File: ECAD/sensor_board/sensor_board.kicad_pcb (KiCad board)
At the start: 2 copper layers, 33 parts, among them J2 Conn_01x04, J4 S4B-XH-SM4-TB, Q2 Q_PMOS_GSD, Q3 Q_PMOS_GSD, Q4 2N7002, U1 TPL5111, U2 TPS22917DBV, U3 TC2030, U4 BC805M, Y1 32.768kHz

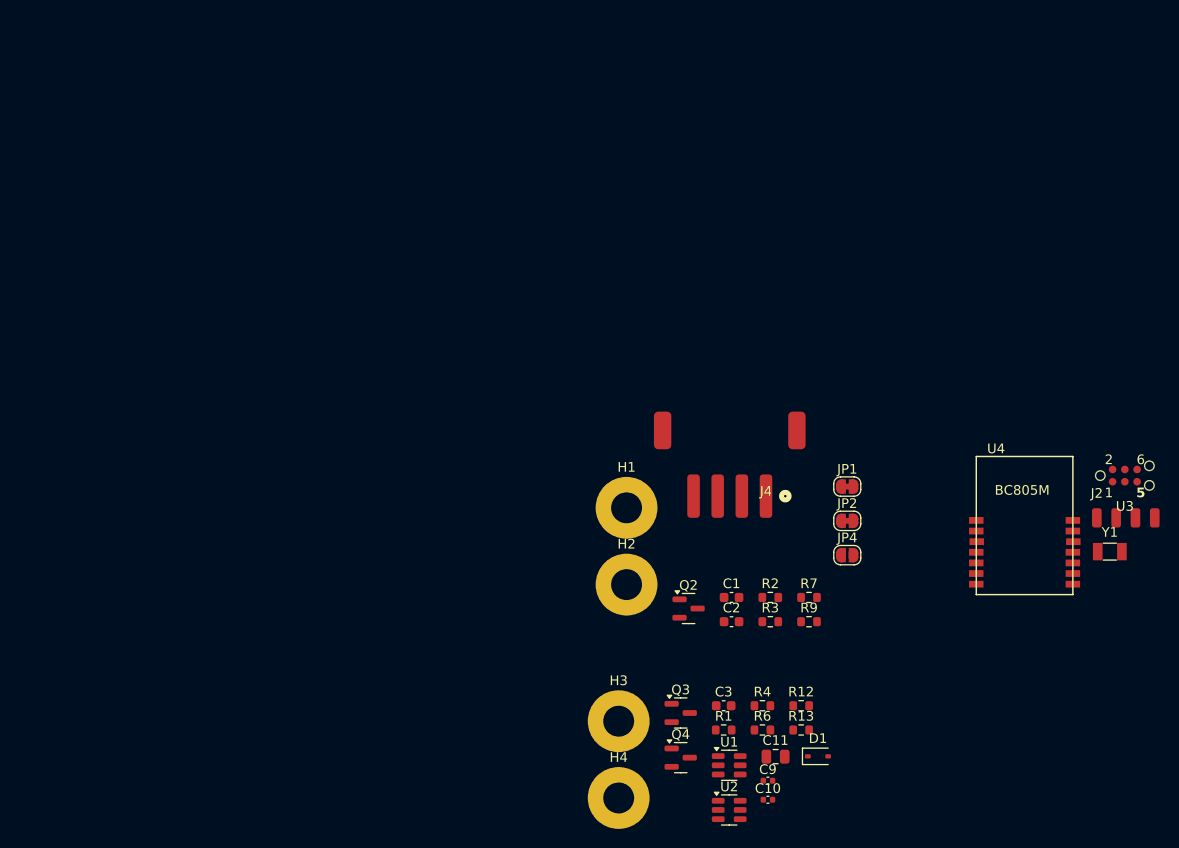
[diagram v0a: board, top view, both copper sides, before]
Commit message: Initial version of routed board
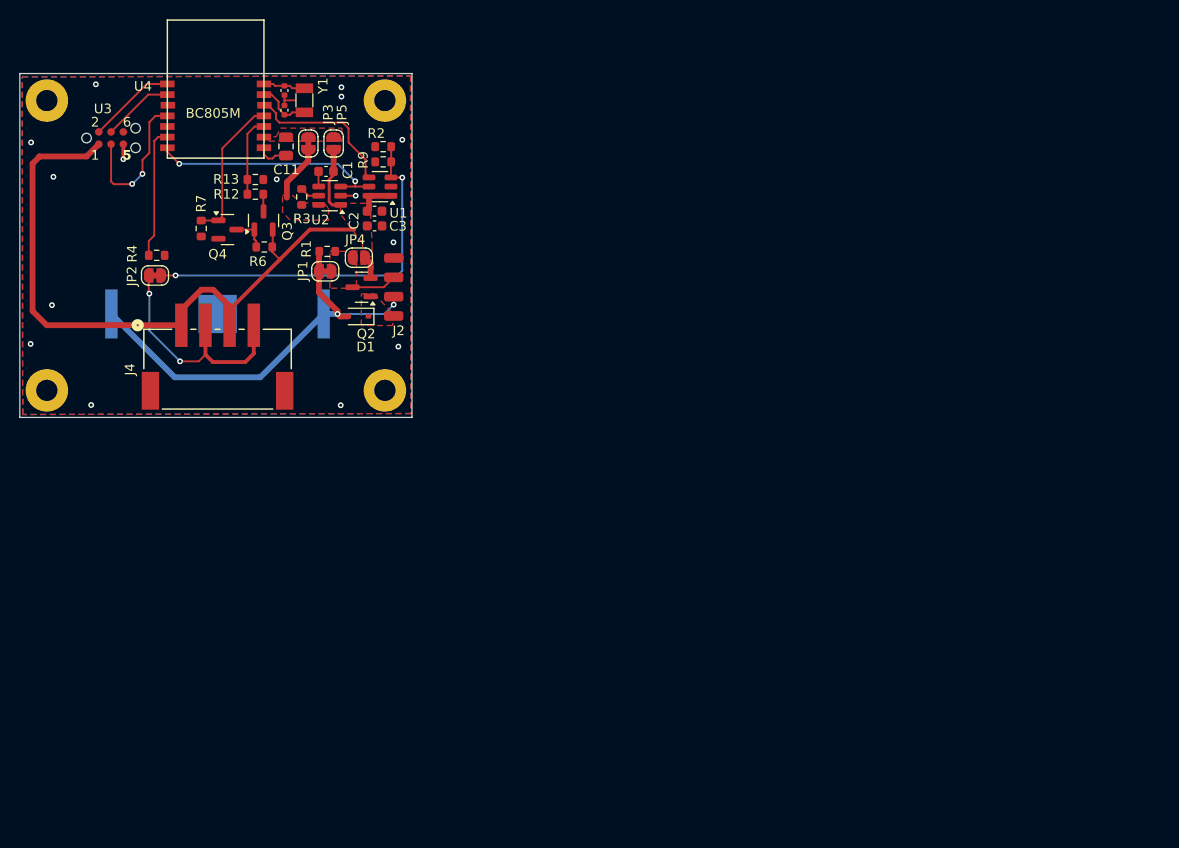
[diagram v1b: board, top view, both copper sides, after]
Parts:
- added BT2: 3034TR, 3034TR:BAT_3034TR, B.Cu at (20.5, 24.9)
- added JP3: ~, Jumper:SolderJumper-2_P1.3mm_Bridged_RoundedPad1.0x1.5mm, F.Cu at (29.9, 7.24)
- added JP5: ~, Jumper:SolderJumper-2_P1.3mm_Open_RoundedPad1.0x1.5mm, F.Cu at (32.5, 7.24)
- H1, H2, H3, H4: footprint MountingHole:MountingHole_3.2mm_M3_Pad -> MountingHole:MountingHole_2.2mm_M2_Pad
- J4: footprint FloMon:S4B-XH-SM4-TB -> FloMon:CONN4_S4B-XH_JST
- moved U3 110.6 mm to (9.45, 6.68)
- moved Y1 95.6 mm to (29.5, 2.77), turned to 90 degrees
- moved U4 95.2 mm to (15.3, 8.76)
- moved C10 88.9 mm to (27.4, 1.76), turned to 90 degrees
- moved C9 85.6 mm to (27.4, 3.79), turned to -90 degrees
- moved C11 81.0 mm to (27.6, 7.54), turned to -90 degrees
- moved R13 80.3 mm to (24.4, 11.0)
- moved R4 78.1 mm to (14.2, 18.8)
- moved R12 77.4 mm to (24.4, 12.5), turned to 180 degrees
- moved JP2 76.0 mm to (14.0, 20.9), turned to 180 degrees
- moved U2 75.9 mm to (32.1, 12.6), turned to 180 degrees
- moved J2 75.7 mm to (38.7, 25.1), turned to 90 degrees
- moved R7 73.6 mm to (18.8, 16.0), turned to -90 degrees
- moved H1 73.3 mm to (2.80, 2.80)
- moved Q4 72.0 mm to (21.5, 16.2)
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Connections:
- C11 pad 1: PWR_GATED -> /VDD
- U1 pad 5: Net-(U1-~{DRV}) -> /NDRV
- U2 pad 3: Net-(U1-~{DRV}) -> /NDRV
- U4 pad 5: /FLOW_SENSE -> unconnected-(U4-P0.18-Pad5)
- U4 pad 6: unconnected-(U4-P0.16-Pad6) -> /FLOW_SENSE
- U4 pad 7: unconnected-(U4-P0.12-Pad7) -> /NDRV
- U4 pad 9: PWR_GATED -> /VDD
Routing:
- net +BATT: track 0.00 -> 83.7 mm
- net Net-(D1-A2): track 0.00 -> 44.4 mm, vias 0 -> 2
- net Net-(JP2-A): track 0.00 -> 39.2 mm, vias 0 -> 2
- net /FLOW_SENSE: track 0.00 -> 38.4 mm, vias 0 -> 2
- net /NDRV: track 0.00 -> 24.6 mm, vias 0 -> 2
- net /DONE_SIGNAL: track 0.00 -> 16.0 mm
- net Net-(U3-NRST): track 0.00 -> 15.5 mm, vias 0 -> 2
- net /SENSE_CTRL: track 0.00 -> 15.1 mm
- net Net-(U3-SWDIO/TMS): track 0.00 -> 9.15 mm
- net GND: track 0.00 -> 8.50 mm, vias 0 -> 15
- net /BATT_DIV: track 0.00 -> 8.28 mm
- net Net-(U3-SWCLK/TCK): track 0.00 -> 7.43 mm
- net PWR_GATED: track 0.00 -> 5.88 mm
- net /Xa: track 0.00 -> 5.59 mm
- net Net-(J2-Pin_3): track 0.00 -> 4.71 mm
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- added copper zone on F.Cu, net +BATT
- added copper zone on F.Cu, net /VDD
- added copper zone on B.Cu, net GND
- added copper zone on F.Cu, net GND
- added copper zone on F.Cu, net Net-(J2-Pin_3)
- added copper zone on F.Cu, net PWR_GATED
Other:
- board outline added: 40.6 x 35.6 mm

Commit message: Updated board layout
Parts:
- moved JP2 25.4 mm to (33.5, 4.55), turned to 90 degrees
- moved R4 24.9 mm to (32.6, 2.08), turned to 180 degrees
- moved R13 22.1 mm to (4.58, 20.9), turned to 180 degrees
- moved R6 22.0 mm to (3.66, 13.9), turned to 0 degrees
- moved Q3 21.5 mm to (3.73, 16.6), turned to -90 degrees
- moved R12 21.0 mm to (4.58, 19.4), turned to 0 degrees
- moved Q4 14.0 mm to (7.47, 15.7), turned to 180 degrees
- moved JP5 11.1 mm to (25.2, 15.6), turned to 180 degrees
- moved R7 8.60 mm to (10.2, 15.8), turned to 90 degrees
- moved JP3 7.41 mm to (25.2, 13.0), turned to 180 degrees
- moved C11 5.50 mm to (22.2, 8.69)
- moved U4 5.15 mm to (10.2, 9.90)
- moved BT2 5.00 mm to (20.3, 19.9)
- moved J4 5.00 mm to (20.3, 25.6)
- moved H3 5.00 mm to (2.80, 27.8)
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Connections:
- U4 pad 10: /BATT_DIV -> /NDRV
- U4 pad 11: /SENSE_CTRL -> /DONE_SIGNAL
- U4 pad 12: /DONE_SIGNAL -> /FLOW_SENSE
- U4 pad 6: /FLOW_SENSE -> /BATT_DIV
- U4 pad 7: /NDRV -> /SENSE_CTRL
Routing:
- net /FLOW_SENSE: track 38.4 -> 69.9 mm, vias 2 -> 0
- net Net-(JP2-A): track 39.2 -> 7.89 mm, vias 2 -> 0
- net /BATT_DIV: track 8.28 -> 20.9 mm
- net +BATT: track 83.7 -> 74.3 mm
- net Net-(D1-A2): track 44.4 -> 53.2 mm, vias 2 -> 4
- net /NDRV: track 24.6 -> 18.1 mm, vias 2 -> 0
- net PWR_GATED: track 5.88 -> 0.00 mm
- net GND: track 8.50 -> 3.67 mm, vias 15 -> 22
- net Net-(U3-NRST): track 15.5 -> 19.2 mm, vias 2 -> 0
- net /SENSE_CTRL: track 15.1 -> 11.9 mm
- net Net-(U3-SWDIO/TMS): track 9.15 -> 8.09 mm
- net /DONE_SIGNAL: track 16.0 -> 17.1 mm
- net Net-(U3-SWCLK/TCK): track 7.43 -> 8.38 mm
- net /Xb: track 4.37 -> 5.06 mm
- net /Xa: track 5.59 -> 5.06 mm
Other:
- board size 40.6 x 35.6 mm -> 40.6 x 30.6 mm

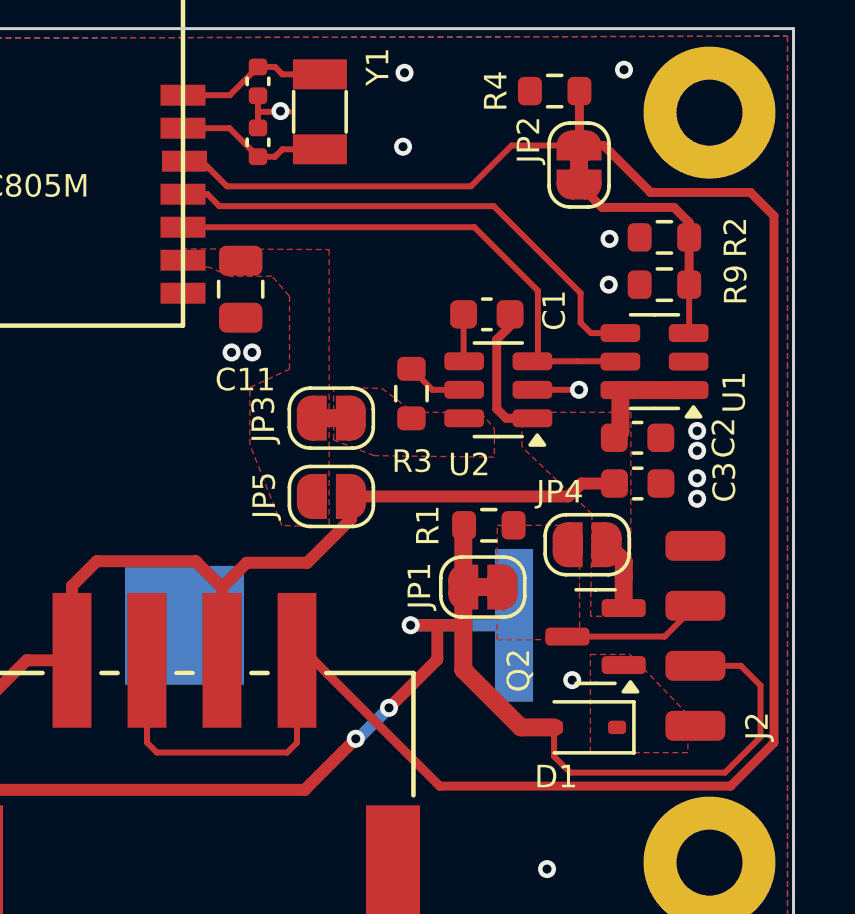
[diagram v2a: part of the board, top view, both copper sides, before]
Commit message: Additional minor changes to layout
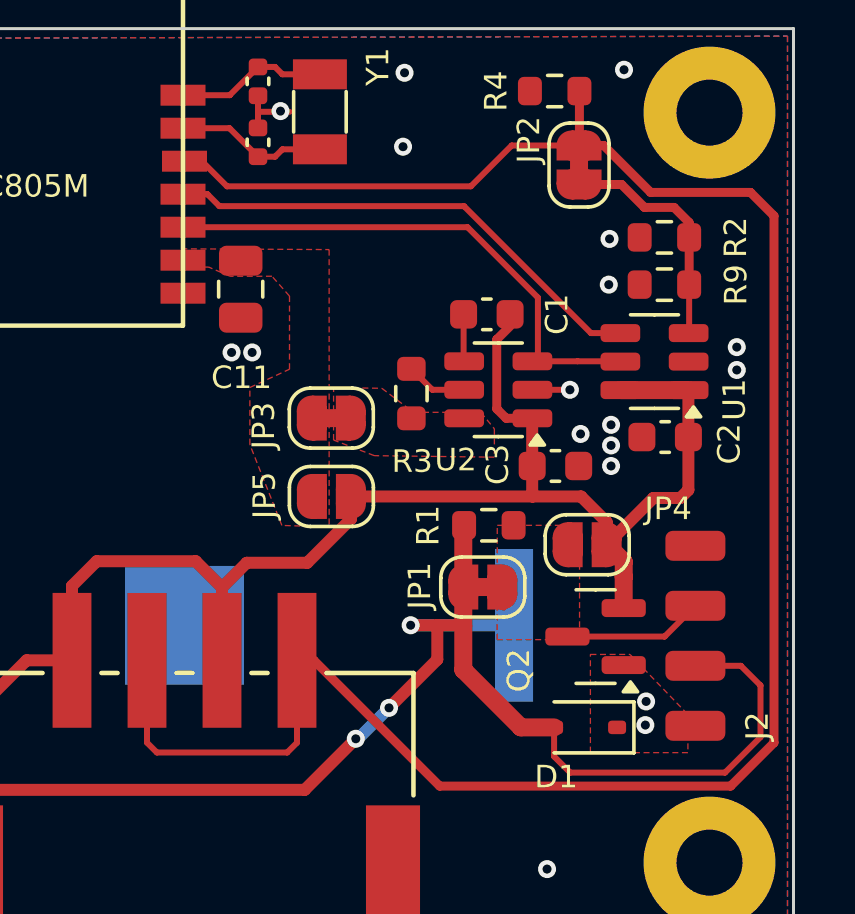
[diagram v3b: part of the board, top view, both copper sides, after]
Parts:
- moved C3 2.80 mm to (32.7, 14.6)
- moved C2 0.92 mm to (36.3, 13.6), turned to 180 degrees
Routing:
- net +BATT: track 74.3 -> 82.7 mm
- net /DONE_SIGNAL: track 17.1 -> 16.5 mm
- net GND: track 3.67 -> 3.37 mm, vias 22 -> 25
- removed copper zone on F.Cu, net +BATT

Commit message: Pushing completed layout
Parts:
- added G***: LOGO, logo:logo_symbol, F.Cu at (17.7, 14.6)
- JP1: value ~ -> Sold_Jump_C
- JP4: value SolderJumper_2_Open -> Sold_Jump_O
- Q2, Q3: value Q_PMOS_GSD -> PMV48XP
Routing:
- net GND: vias 25 -> 34
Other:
- board text added: "---- FM-001A ----"
